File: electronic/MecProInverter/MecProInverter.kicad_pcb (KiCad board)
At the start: 4 copper layers, 104 x 168 mm, 184 parts, among them J10 Net, J3 ISO_Data, J4 Motor, J5 Display, J6 MAX312820, J7 Test, J8 U_ZK, J9 U_VS, K2 RT314A12, Q1 DMN3404L, Q2 DMN3404L, SW1 PTS645SM95SMTR92LFS, SW2 PTS645SM95SMTR92LFS, SW3 PTS645SM95SMTR92LFS, U1 ESP32-S3-MINI-1-N8, U10 CC6904SO-30A, U11 CC6904SO-30A, U12 TEA1-0505HI, U13 IKCM20L60GA, U14 PSRV05-4MR6T1G, U15 ADUM1201ARZ-RL7, U16 ADUM1201ARZ-RL7, U17 PSRV05-4MR6T1G, U18 PMV100EPAR, U19 PSRV05-4MR6T1G, U2 ADUM3160, U20 PSRV05-4MR6T1G, U21 RK09D113000F_10k, U3 TYPE-C_16PIN_2MD(073), U4 LVE2560E, U5 TPS563201DDCR, U6 SKRKAEE020, U7 SKRKAEE020, U8 TLA2528IRTER, U9 CC6904SO-30A

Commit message: Electronic
Added USB-C CC Resistor
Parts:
- added R66: 5.1k, Resistor_SMD:R_0603_1608Metric, F.Cu at (27.6, 110.2)
- added R67: 5.1k, Resistor_SMD:R_0603_1608Metric, F.Cu at (27.6, 112.8)
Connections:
- U3 pad 10: unconnected-(U3-CC2-Pad10) -> Net-(U3-CC2)
- U3 pad 4: unconnected-(U3-CC1-Pad4) -> Net-(U3-CC1)
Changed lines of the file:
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@@
   (net 67 "Net-(U2-PIN)")
   (net 68 "unconnected-(U3-SBU2-Pad3)")
-  (net 69 "unconnected-(U3-CC1-Pad4)")
+  (net 69 "Net-(U3-CC2)")
   (net 70 "Net-(U3-DN1)")
   (net 71 "Net-(U3-DP1)")
   (net 72 "unconnected-(U3-SBU1-Pad9)")
-  (net 73 "unconnected-(U3-CC2-Pad10)")
+  (net 73 "Net-(U3-CC1)")
   (net 74 "Net-(U8-AIN1{slash}GPIO1)")
   (net 75 "Net-(U5-SW)")
@@
     )
   )
+  (footprint "Resistor_SMD:R_0603_1608Metric" (layer "F.Cu")
+    (at 27.575 110.24)
+    (descr "Resistor SMD 0603 (1608 Metric), square (rectangular) end terminal, IPC_7351 nominal, (Body size source: IPC-SM-782 page 72, https://www.pcb-3d.com/wordpress/wp-content/uploads/ipc-sm-782a_amendment_1_and_2.pdf), generated with kicad-footprint-generator")
+    (tags "resistor")
+    (property "Sheetfile" "control.kicad_sch")
+    (property "Sheetname" "Control")
+    (property "ki_description" "Resistor")
+    (property "ki_keywords" "R res resistor")
+    (attr smd)
+    (fp_text reference "R66" (at 0 -1.43) (layer "F.SilkS")
+        (effects (font (size 1 1) (thickness 0.15)))
+    )
+    (fp_text value "5.1k" (at 0 1.43) (layer "F.Fab")
+        (effects (font (size 1 1) (thickness 0.15)))
+    )
+    (fp_text user "${REFERENCE}" (at 0 0) (layer "F.Fab")
+        (effects (font (size 0.4 0.4) (thickness 0.06)))
+    )
+    (fp_line (start -0.237258 -0.5225) (end 0.237258 -0.5225)
+      (stroke (width 0.12) (type solid)) (layer "F.SilkS"))
+    (fp_line (start -0.237258 0.5225) (end 0.237258 0.5225)
+      (stroke (width 0.12) (type solid)) (layer "F.SilkS"))
+    (fp_line (start -1.48 -0.73) (end 1.48 -0.73)
+      (stroke (width 0.05) (type solid)) (layer "F.CrtYd"))
+    (fp_line (start -1.48 0.73) (end -1.48 -0.73)
+      (stroke (width 0.05) (type solid)) (layer "F.CrtYd"))
+    (fp_line (start 1.48 -0.73) (end 1.48 0.73)
+      (stroke (width 0.05) (type solid)) (layer "F.CrtYd"))
+    (fp_line (start 1.48 0.73) (end -1.48 0.73)
+      (stroke (width 0.05) (type solid)) (layer "F.CrtYd"))
+    (fp_line (start -0.8 -0.4125) (end 0.8 -0.4125)
+      (stroke (width 0.1) (type solid)) (layer "F.Fab"))
+    (fp_line (start -0.8 0.4125) (end -0.8 -0.4125)
+      (stroke (width 0.1) (type solid)) (layer "F.Fab"))
+    (fp_line (start 0.8 -0.4125) (end 0.8 0.4125)
+      (stroke (width 0.1) (type solid)) (layer "F.Fab"))
+    (fp_line (start 0.8 0.4125) (end -0.8 0.4125)
+      (stroke (width 0.1) (type solid)) (layer "F.Fab"))
+    (pad "1" smd roundrect (at -0.825 0) (size 0.8 0.95) (layers "F.Cu" "F.Paste" "F.Mask") (roundrect_rratio 0.25)
+      (net 69 "Net-(U3-CC2)") (pintype "passive"))
+    (pad "2" smd roundrect (at 0.825 0) (size 0.8 0.95) (layers "F.Cu" "F.Paste" "F.Mask") (roundrect_rratio 0.25)
+      (net 127 "GNDD") (pintype "passive"))
+    (model "${KICAD6_3DMODEL_DIR}/Resistor_SMD.3dshapes/R_0603_1608Metric.wrl"
+      (offset (xyz 0 0 0))
+      (scale (xyz 1 1 1))
+      (rotate (xyz 0 0 0))
+    )
+  )
   (footprint "footprint:KEY-SMD_4P-L6.1-W6.1-P4.50-LS9.0" locked (layer "F.Cu")
     (at 119 64)
@@
       (net 68 "unconnected-(U3-SBU2-Pad3)") (pinfunction "SBU2") (pintype "unspecified+no_connect"))
     (pad "4" smd rect locked (at -1.249809 -2.375032) (size 0.3 1.1) (layers "F.Cu" "F.Paste" "F.Mask")
-      (net 69 "unconnected-(U3-CC1-Pad4)") (pinfunction "CC1") (pintype "unspecified+no_connect"))
+      (net 73 "Net-(U3-CC1)") (pinfunction "CC1") (pintype "unspecified"))
     (pad "5" smd rect locked (at -0.749936 -2.375032) (size 0.3 1.1) (layers "F.Cu" "F.Paste" "F.Mask")
       (net 70 "Net-(U3-DN1)") (pinfunction "DN2") (pintype "unspecified"))
@@
       (net 72 "unconnected-(U3-SBU1-Pad9)") (pinfunction "SBU1") (pintype "unspecified+no_connect"))
     (pad "10" smd rect locked (at 1.750191 -2.375032) (size 0.3 1.1) (layers "F.Cu" "F.Paste" "F.Mask")
-      (net 73 "unconnected-(U3-CC2-Pad10)") (pinfunction "CC2") (pintype "unspecified+no_connect"))
+      (net 69 "Net-(U3-CC2)") (pinfunction "CC2") (pintype "unspecified"))
     (pad "11" smd rect locked (at 2.400178 -2.375032) (size 0.6 1.1) (layers "F.Cu" "F.Paste" "F.Mask")
       (net 126 "+5VD") (pinfunction "VBUS") (pintype "unspecified"))
@@
       (offset (xyz 0 0 0))
       (scale (xyz 1 1 1))
+      (rotate (xyz 0 0 0))
+    )
+  )
+  (footprint "Resistor_SMD:R_0603_1608Metric" (layer "F.Cu")
+    (at 27.575 112.75)
+    (descr "Resistor SMD 0603 (1608 Metric), square (rectangular) end terminal, IPC_7351 nominal, (Body size source: IPC-SM-782 page 72, https://www.pcb-3d.com/wordpress/wp-content/uploads/ipc-sm-782a_amendment_1_and_2.pdf), generated with kicad-footprint-generator")
+    (tags "resistor")
+    (property "Sheetfile" "control.kicad_sch")
+    (property "Sheetname" "Control")
+    (property "ki_description" "Resistor")
+    (property "ki_keywords" "R res resistor")
+    (attr smd)
+    (fp_text reference "R67" (at 0 -1.43) (layer "F.SilkS")
+        (effects (font (size 1 1) (thickness 0.15)))
+    )
+    (fp_text value "5.1k" (at 0 1.43) (layer "F.Fab")
+        (effects (font (size 1 1) (thickness 0.15)))
+    )
+    (fp_text user "${REFERENCE}" (at 0 0) (layer "F.Fab")
+        (effects (font (size 0.4 0.4) (thickness 0.06)))
+    )
+    (fp_line (start -0.237258 -0.5225) (end 0.237258 -0.5225)
+      (stroke (width 0.12) (type solid)) (layer "F.SilkS"))
+    (fp_line (start -0.237258 0.5225) (end 0.237258 0.5225)
+      (stroke (width 0.12) (type solid)) (layer "F.SilkS"))
+    (fp_line (start -1.48 -0.73) (end 1.48 -0.73)
+      (stroke (width 0.05) (type solid)) (layer "F.CrtYd"))
+    (fp_line (start -1.48 0.73) (end -1.48 -0.73)
+      (stroke (width 0.05) (type solid)) (layer "F.CrtYd"))
+    (fp_line (start 1.48 -0.73) (end 1.48 0.73)
+      (stroke (width 0.05) (type solid)) (layer "F.CrtYd"))
+    (fp_line (start 1.48 0.73) (end -1.48 0.73)
+      (stroke (width 0.05) (type solid)) (layer "F.CrtYd"))
+    (fp_line (start -0.8 -0.4125) (end 0.8 -0.4125)
+      (stroke (width 0.1) (type solid)) (layer "F.Fab"))
+    (fp_line (start -0.8 0.4125) (end -0.8 -0.4125)
+      (stroke (width 0.1) (type solid)) (layer "F.Fab"))
+    (fp_line (start 0.8 -0.4125) (end 0.8 0.4125)
+      (stroke (width 0.1) (type solid)) (layer "F.Fab"))
+    (fp_line (start 0.8 0.4125) (end -0.8 0.4125)
+      (stroke (width 0.1) (type solid)) (layer "F.Fab"))
+    (pad "1" smd roundrect (at -0.825 0) (size 0.8 0.95) (layers "F.Cu" "F.Paste" "F.Mask") (roundrect_rratio 0.25)
+      (net 73 "Net-(U3-CC1)") (pintype "passive"))
+    (pad "2" smd roundrect (at 0.825 0) (size 0.8 0.95) (layers "F.Cu" "F.Paste" "F.Mask") (roundrect_rratio 0.25)
+      (net 127 "GNDD") (pintype "passive"))
+    (model "${KICAD6_3DMODEL_DIR}/Resistor_SMD.3dshapes/R_0603_1608Metric.wrl"
+      (offset (xyz 0 0 0))
+      (scale (xyz 1 1 1))

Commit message: Electronic
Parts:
- moved R37 186.9 mm to (162.6, 210.3)
- moved R36 186.8 mm to (162.6, 208.3), turned to 180 degrees
- moved D1 167.9 mm to (148.2, 218.8)
- moved D2 167.9 mm to (150.2, 218.8)
- moved R13 156.3 mm to (148.2, 215.5), turned to -90 degrees
- moved R14 156.0 mm to (150.2, 215.4), turned to -90 degrees
- moved U17 11.7 mm to (178.7, 200.8), turned to 180 degrees
- moved U14 6.62 mm to (166.4, 210.3)
- moved U15 0.44 mm to (184.7, 200.3)
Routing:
- net +5VD: track 0.00 -> 7.11 mm
- net GND: track 0.00 -> 3.55 mm, vias 0 -> 1
- net Net-(U3-DP1): track 0.00 -> 3.27 mm
- net Net-(U3-DN1): track 0.00 -> 3.03 mm, vias 0 -> 1
- net GNDD: track 0.00 -> 2.71 mm
- net Net-(D2-A): track 0.00 -> 1.71 mm
- net Net-(D1-A): track 0.00 -> 1.64 mm

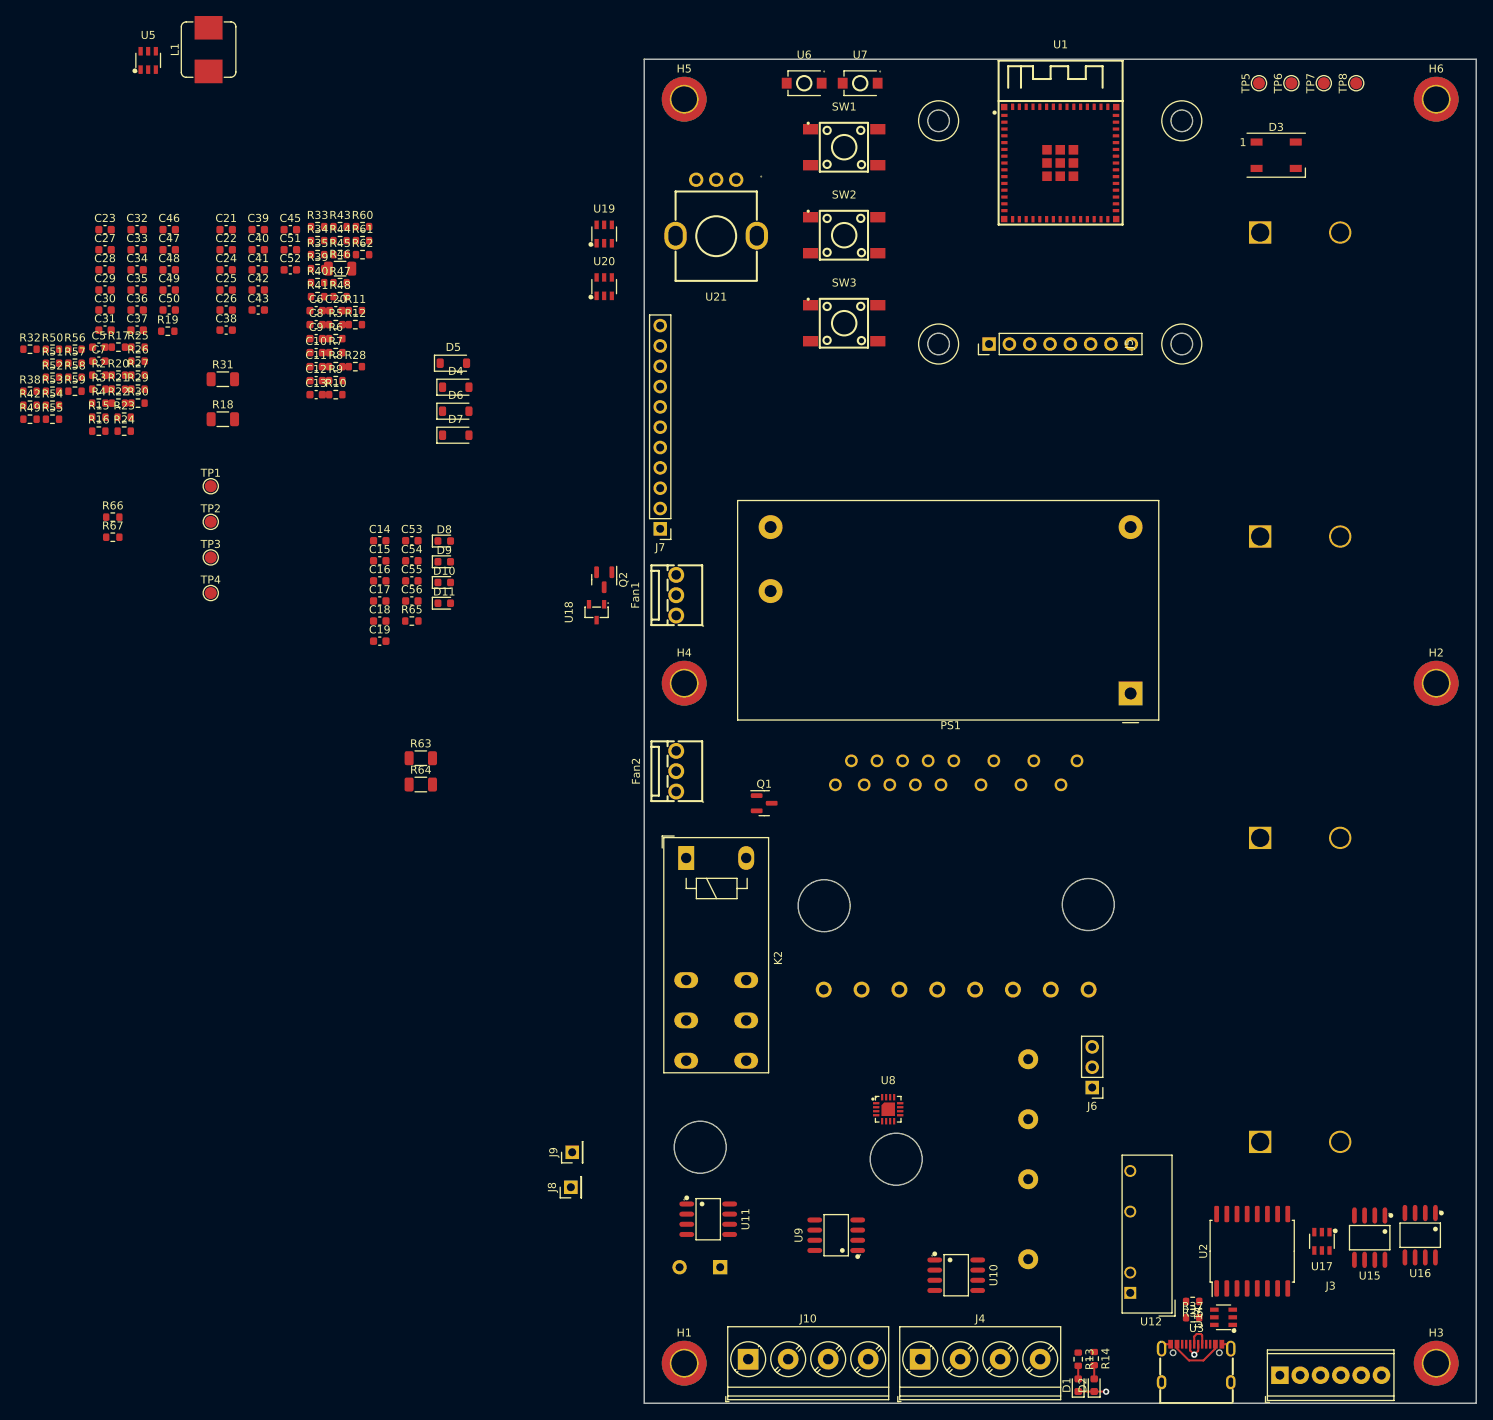
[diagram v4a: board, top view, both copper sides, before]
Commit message: Electronic
Layout begin
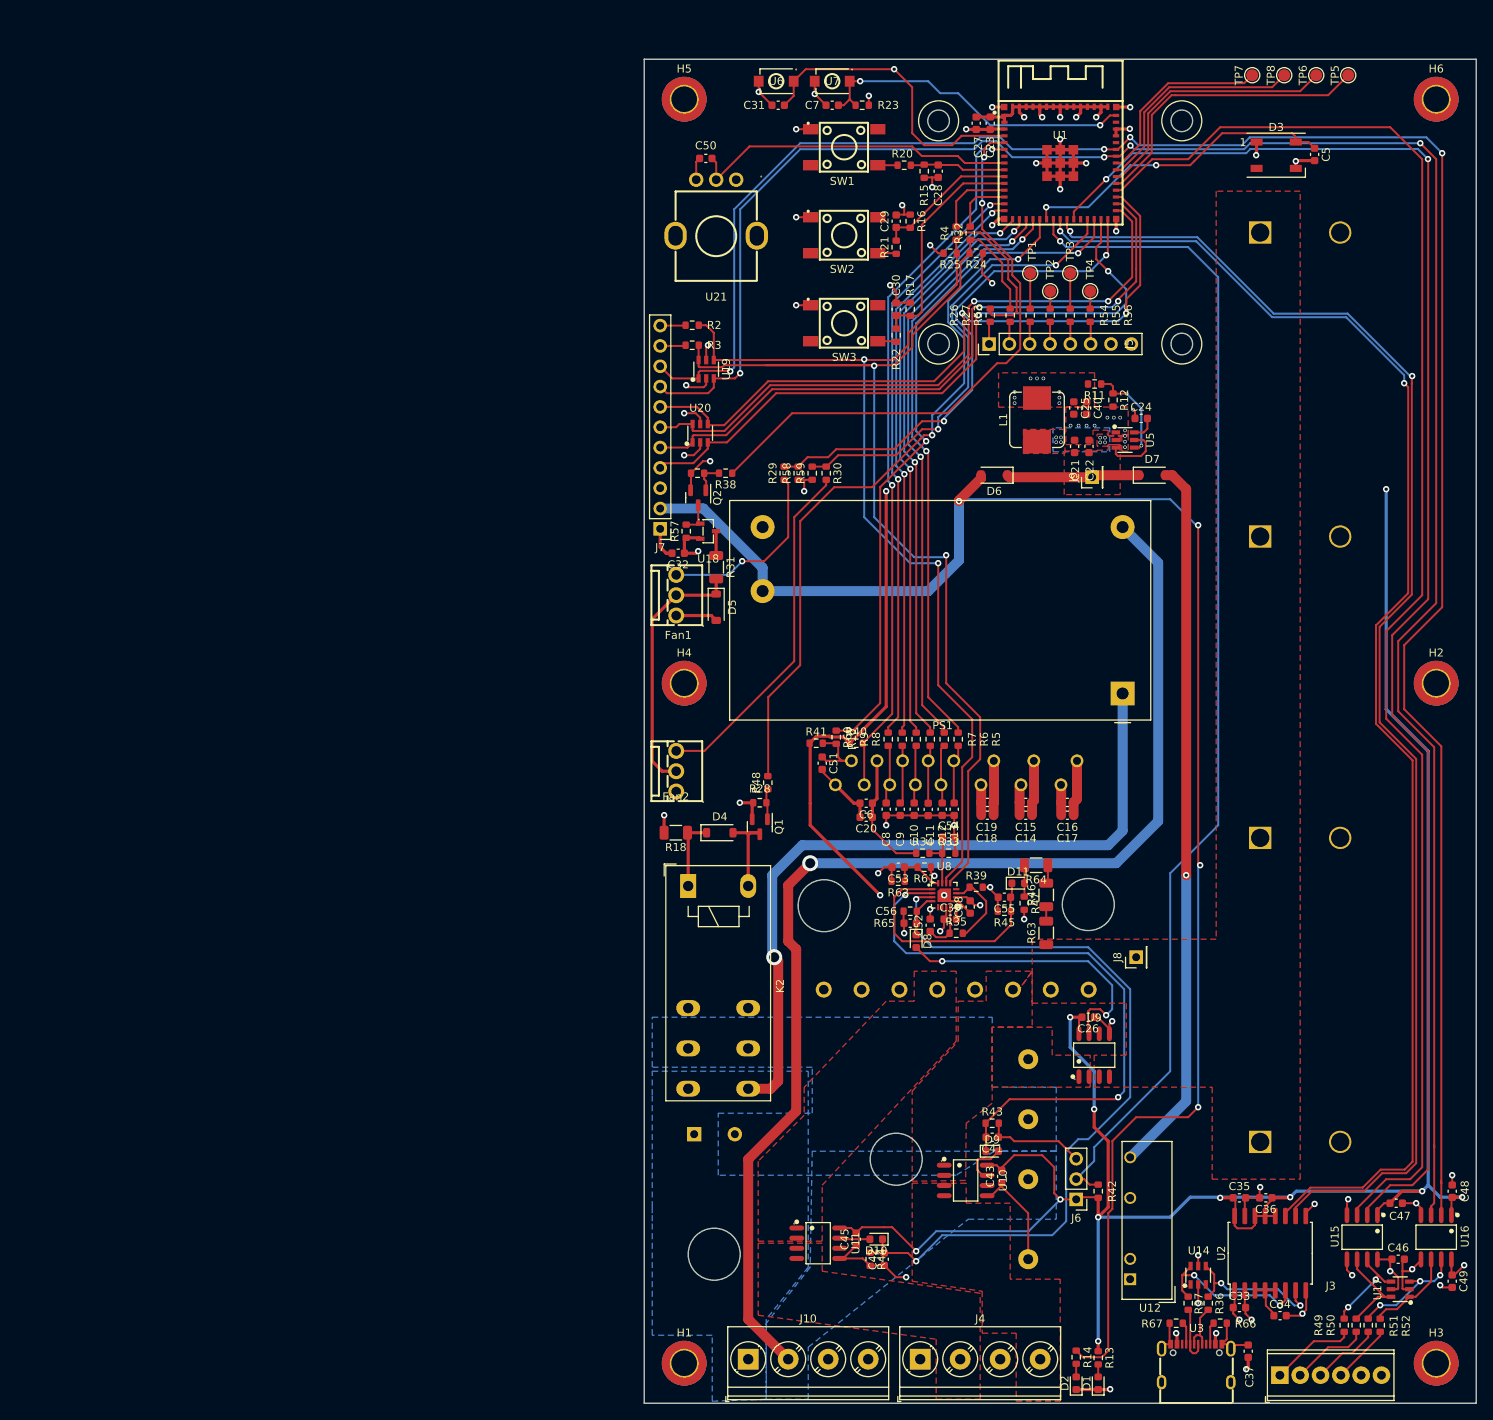
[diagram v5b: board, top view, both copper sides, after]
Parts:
- moved R52 203.9 mm to (186.0, 211.2), turned to -90 degrees
- moved R51 203.7 mm to (184.5, 211.2), turned to -90 degrees
- moved R50 203.6 mm to (183.0, 211.2), turned to -90 degrees
- moved C49 202.7 mm to (195.0, 205.8), turned to -90 degrees
- moved C46 200.4 mm to (188.2, 203.0)
- moved R49 199.5 mm to (181.5, 211.2), turned to 90 degrees
- moved C48 197.4 mm to (195.0, 194.5), turned to 90 degrees
- moved C47 194.2 mm to (188.0, 196.0)
- moved C34 193.7 mm to (173.5, 210.1)
- moved C33 191.0 mm to (168.4, 209.0)
- moved C37 188.6 mm to (169.5, 214.5), turned to 90 degrees
- moved C36 179.5 mm to (171.7, 195.3), turned to 180 degrees
- moved C35 178.5 mm to (168.4, 195.3)
- moved R66 171.2 mm to (166.0, 211.0)
- moved R42 165.8 mm to (150.8, 194.5), turned to 90 degrees
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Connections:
- net /Control/USB_DN renamed /Control/USB_N
- net /Control/USB_DP renamed /Control/USB_P
- C35 pad 1: Net-(U2-PIN) -> +3.3V
- U2 pad 12: Net-(U2-PIN) -> +3.3V
- U2 pad 13: Net-(U2-PIN) -> +3.3V
- U2 pad 14: Net-(U2-PIN) -> +3.3V
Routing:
- net +3.3V: track 0.00 -> 365.3 mm, vias 0 -> 37
- net /Control/UART_RX: track 0.00 -> 262.7 mm, vias 0 -> 4
- net /Control/UART_TX: track 0.00 -> 262.1 mm, vias 0 -> 4
- net +15V: track 0.00 -> 229.7 mm, vias 0 -> 6
- net /Control/ISO_GPIO_1: track 0.00 -> 190.0 mm, vias 0 -> 2
- net /Control/ISO_GPIO_2: track 0.00 -> 184.0 mm
- net GND: track 3.55 -> 181.1 mm, vias 1 -> 44
- net /Control/USB_N: track 0.00 -> 173.0 mm, vias 0 -> 2
- net /Control/USB_P: track 0.00 -> 172.6 mm, vias 0 -> 2
- net /Power/AC_N: track 0.00 -> 152.6 mm, vias 0 -> 1
- net /Control/TEMP_HEATSINK: track 0.00 -> 147.8 mm, vias 0 -> 1
- net I2C_SCL: track 0.00 -> 146.0 mm, vias 0 -> 2
- net I2C_SDA: track 0.00 -> 140.3 mm, vias 0 -> 2
- net Net-(D10-K): track 0.00 -> 97.7 mm, vias 0 -> 2
- net /Power/AC_L: track 0.00 -> 93.5 mm, vias 0 -> 1
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- added copper zone on In2.Cu, net +15V
- added copper zone on F.Cu, net +3.3V
- added copper zone on In2.Cu, net +3.3V
- added copper zone on In2.Cu, net +5VD
- added copper zone on B.Cu, net /Power/AC_L
- added copper zone on B.Cu, net /Power/AC_N
- added copper zone on F.Cu, net /Power/U
- added copper zone on In1.Cu, net /Power/V
- added copper zone on In2.Cu, net /Power/V
- added copper zone on F.Cu, net /Power/W
- added copper zone on F.Cu, net GND
- added copper zone on In1.Cu, net GND
- added copper zone on In1.Cu, net GNDD
- added copper zone on In1.Cu, net GNDS
- added copper zone on F.Cu, net Net-(J8-Pin_1)
- added copper zone on F.Cu, net Net-(U13-U)
- added copper zone on F.Cu, net Net-(U13-W)
- added copper zone on F.Cu, net Net-(U4-VDD)
- added copper zone on B.Cu, net Net-(U4-~Phase)
- added copper zone on B.Cu, net Net-(U5-SW)
- added copper zone on F.Cu, net Net-(U5-SW)
- added copper zone on F.Cu, net VS
- added copper zone on In2.Cu, net VSS
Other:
- rule pad_to_mask_clearance: 0 -> 0.038

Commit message: Electronic
Generated Step
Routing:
- net Net-(U1-IO39): track 37.4 -> 34.6 mm
- net Net-(U1-IO40): track 32.9 -> 30.3 mm
- net Net-(U1-IO41): track 28.4 -> 25.9 mm
- net Net-(U1-IO0): track 38.2 -> 37.1 mm
- net GND: track 181.1 -> 182.1 mm
- net GNDS: track 11.6 -> 12.6 mm
- net VSS: track 11.1 -> 11.9 mm
- net Net-(U1-IO42): track 24.0 -> 23.3 mm
- added copper zone on In2.Cu, net Earth
- added copper zone on B.Cu, net GND
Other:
- rule pad_to_mask_clearance: 0.038 -> 0

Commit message: Electronic
Ready to buy
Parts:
- removed D1: LED_3.3V, LED_SMD:LED_0603_1608Metric
- removed D2: LED_15V, LED_SMD:LED_0603_1608Metric
- added D15V1: LED_15V, LED_SMD:LED_0603_1608Metric, F.Cu at (148.0, 218.4)
- added D3V3: LED_3.3V, LED_SMD:LED_0603_1608Metric, F.Cu at (150.8, 218.5)
- moved C41 0.85 mm to (136.7, 187.7)
- moved D9 0.85 mm to (136.7, 189.4)
- moved R43 0.85 mm to (136.7, 185.9)
- moved C43 0.83 mm to (137.8, 192.7)
- moved U10 0.83 mm to (133.3, 193.2)
- renumbered U6 to Boot, U7 to Reset
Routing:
- net +3.3V: track 365.3 -> 207.8 mm, vias 37 -> 35
- net VS: track 24.2 -> 8.52 mm
- net +5VD: track 9.82 -> 14.6 mm
- net /Control/ISO_GPIO_1: track 190.0 -> 186.3 mm
- net /Control/USB_N: track 173.0 -> 169.5 mm
- net /Control/USB_P: track 172.6 -> 169.1 mm
- net /Control/ISO_GPIO_2: track 184.0 -> 180.8 mm
- net /Control/FAN_CONTROL: track 72.4 -> 74.6 mm
- net +15V: track 229.7 -> 227.9 mm
- net GND: track 182.1 -> 183.5 mm, vias 44 -> 45
- net /Control/SPI_MOSI: track 81.0 -> 82.4 mm
- net Net-(D10-K): track 97.7 -> 96.6 mm
- net ITRIP: track 86.3 -> 87.3 mm
- net Net-(D9-K): track 76.4 -> 77.2 mm
- net /Control/SPI_CLK: track 83.3 -> 84.0 mm
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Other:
- outline, holes or cut-outs redrawn
- board text added: "15V"
- board text added: "3,6kW Inverter"
- board text added: "3V3"
- board text added: "AC_L"
- board text added: "AC_N"
- board text added: "Created by: Fabian Hofmann Martin Sölkner Lukas Jansen Yu Hsuan"
- board text added: "DATA"
- board text added: "GND"
- board text added: "GNDS"
- board text added: "GPIO_21"
- board text added: "GPIO_38"
- board text added: "I2C_CLK"
- board text added: "I2C_SDA"
- board text added: "MecProInverter"
- board text added: "PE"
- board text added: "SPI_CLK"
- board text added: "SPI_CS"
- board text added: "SPI_MISO"
- board text added: "SPI_MOSI"
- board text added: "U"
- board text added: "UART_RX"
- board text added: "UART_TX"
- board text added: "V"
- board text added: "VS"
- board text added: "VSS"
- board text added: "Version: 1.0 Nennespannung: 230V Frequenz in: 50Hz Nennstrom: 16A Leistung: 3.6kW Frequenz out: 0-500 Hz"
- board text added: "W"
- board text added: "Zwischen Spannung"

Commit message: Electronic
PCB buy!!!
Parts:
- C20, C22, C37: value 10uF -> 22uF
- C38, C39: value 220nF -> 100nF
- R10, R38, R48, R5, R6, R7, R8, R9: value 165 -> 121
- R11: value 33.2k -> 33k
- R13: value 40 -> 121
- R28: value 100k -> 10k
- R41: value 4,7k -> 3,3k
- R49, R50, R51, R52: value 180 -> 121
- renumbered Boot to U6, Reset to U7
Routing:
- net Earth: track 0.00 -> 56.0 mm, vias 0 -> 1
- net /Power/AC_N: track 152.6 -> 172.1 mm
- net (no net): track 32.7 -> 39.6 mm
- net +3.3V: track 207.8 -> 212.1 mm, vias 35 -> 34
- net +15V: track 227.9 -> 226.1 mm
